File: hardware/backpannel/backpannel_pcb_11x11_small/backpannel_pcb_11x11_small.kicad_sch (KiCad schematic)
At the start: 30 parts, among them J1 Conn_01x02_Female, J2 Conn_02x03, U1 AMS1117-3.3, U2 ESP-12E

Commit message: placement 11x11
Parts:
- S1, S10, S11, S2, S3, S4, S5, S6, S7, S8, S9: footprint woordklok_footprint:WS2812_ledstrip_30leds_meter -> woordklok_footprint:WS2812_ledstrip_60leds_meter
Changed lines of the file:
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@@
     (property "Reference" "S11" (id 0) (at 224.79 120.65 0))
     (property "Value" "WS2812_ledstrip" (id 1) (at 225.26 130.81 0))
-    (property "Footprint" "woordklok_footprint:WS2812_ledstrip_30leds_meter" (id 2) (at 227.33 125.73 0)
+    (property "Footprint" "woordklok_footprint:WS2812_ledstrip_60leds_meter" (id 2) (at 227.33 125.73 0)
       (effects (font (size 1.27 1.27)) hide)
     )
@@
     (property "Reference" "S5" (id 0) (at 226.06 118.11 0))
     (property "Value" "WS2812_ledstrip" (id 1) (at 225.59 107.95 0))
-    (property "Footprint" "woordklok_footprint:WS2812_ledstrip_30leds_meter" (id 2) (at 223.52 113.03 0)
+    (property "Footprint" "woordklok_footprint:WS2812_ledstrip_60leds_meter" (id 2) (at 223.52 113.03 0)
       (effects (font (size 1.27 1.27)) hide)
     )
@@
     (property "Reference" "S9" (id 0) (at 224.79 80.01 0))
     (property "Value" "WS2812_ledstrip" (id 1) (at 225.26 90.17 0))
-    (property "Footprint" "woordklok_footprint:WS2812_ledstrip_30leds_meter" (id 2) (at 227.33 85.09 0)
+    (property "Footprint" "woordklok_footprint:WS2812_ledstrip_60leds_meter" (id 2) (at 227.33 85.09 0)
       (effects (font (size 1.27 1.27)) hide)
     )
@@
     (property "Reference" "S8" (id 0) (at 224.79 59.69 0))
     (property "Value" "WS2812_ledstrip" (id 1) (at 225.26 69.85 0))
-    (property "Footprint" "woordklok_footprint:WS2812_ledstrip_30leds_meter" (id 2) (at 227.33 64.77 0)
+    (property "Footprint" "woordklok_footprint:WS2812_ledstrip_60leds_meter" (id 2) (at 227.33 64.77 0)
       (effects (font (size 1.27 1.27)) hide)
     )
@@
     (property "Reference" "S6" (id 0) (at 226.06 138.43 0))
     (property "Value" "WS2812_ledstrip" (id 1) (at 225.59 128.27 0))
-    (property "Footprint" "woordklok_footprint:WS2812_ledstrip_30leds_meter" (id 2) (at 223.52 133.35 0)
+    (property "Footprint" "woordklok_footprint:WS2812_ledstrip_60leds_meter" (id 2) (at 223.52 133.35 0)
       (effects (font (size 1.27 1.27)) hide)
     )
@@
     (property "Reference" "S7" (id 0) (at 226.06 39.37 0))
     (property "Value" "WS2812_ledstrip" (id 1) (at 224.79 49.53 0))
-    (property "Footprint" "woordklok_footprint:WS2812_ledstrip_30leds_meter" (id 2) (at 227.33 44.45 0)
+    (property "Footprint" "woordklok_footprint:WS2812_ledstrip_60leds_meter" (id 2) (at 227.33 44.45 0)
       (effects (font (size 1.27 1.27)) hide)
     )
@@
     (property "Reference" "S1" (id 0) (at 224.79 36.83 0))
     (property "Value" "WS2812_ledstrip" (id 1) (at 226.06 26.67 0))
-    (property "Footprint" "woordklok_footprint:WS2812_ledstrip_30leds_meter" (id 2) (at 223.52 31.75 0)
+    (property "Footprint" "woordklok_footprint:WS2812_ledstrip_60leds_meter" (id 2) (at 223.52 31.75 0)
       (effects (font (size 1.27 1.27)) hide)
     )
@@
     (property "Reference" "S10" (id 0) (at 224.79 100.33 0))
     (property "Value" "WS2812_ledstrip" (id 1) (at 225.26 110.49 0))
-    (property "Footprint" "woordklok_footprint:WS2812_ledstrip_30leds_meter" (id 2) (at 227.33 105.41 0)
+    (property "Footprint" "woordklok_footprint:WS2812_ledstrip_60leds_meter" (id 2) (at 227.33 105.41 0)
       (effects (font (size 1.27 1.27)) hide)
     )
@@
     (property "Reference" "S2" (id 0) (at 226.06 57.15 0))
     (property "Value" "WS2812_ledstrip" (id 1) (at 225.59 46.99 0))
-    (property "Footprint" "woordklok_footprint:WS2812_ledstrip_30leds_meter" (id 2) (at 223.52 52.07 0)
+    (property "Footprint" "woordklok_footprint:WS2812_ledstrip_60leds_meter" (id 2) (at 223.52 52.07 0)
       (effects (font (size 1.27 1.27)) hide)
     )
@@
     (property "Reference" "S4" (id 0) (at 226.06 97.79 0))
     (property "Value" "WS2812_ledstrip" (id 1) (at 225.59 87.63 0))
-    (property "Footprint" "woordklok_footprint:WS2812_ledstrip_30leds_meter" (id 2) (at 223.52 92.71 0)
+    (property "Footprint" "woordklok_footprint:WS2812_ledstrip_60leds_meter" (id 2) (at 223.52 92.71 0)
       (effects (font (size 1.27 1.27)) hide)
     )
@@
     (property "Reference" "S3" (id 0) (at 226.06 77.47 0))
     (property "Value" "WS2812_ledstrip" (id 1) (at 225.59 67.31 0))
-    (property "Footprint" "woordklok_footprint:WS2812_ledstrip_30leds_meter" (id 2) (at 223.52 72.39 0)
+    (property "Footprint" "woordklok_footprint:WS2812_ledstrip_60leds_meter" (id 2) (at 223.52 72.39 0)
       (effects (font (size 1.27 1.27)) hide)
     )
@@
     )
     (path "/d23aa89d-c621-4b1b-a845-8c26429d6622"
-      (reference "S1") (unit 1) (value "WS2812_ledstrip") (footprint "woordklok_footprint:WS2812_ledstrip_30leds_meter")
+      (reference "S1") (unit 1) (value "WS2812_ledstrip") (footprint "woordklok_footprint:WS2812_ledstrip_60leds_meter")
     )
     (path "/e61e3b10-16bb-45fa-9a42-277efd2ec104"
-      (reference "S2") (unit 1) (value "WS2812_ledstrip") (footprint "woordklok_footprint:WS2812_ledstrip_30leds_meter")
+      (reference "S2") (unit 1) (value "WS2812_ledstrip") (footprint "woordklok_footprint:WS2812_ledstrip_60leds_meter")
     )
     (path "/eef9a49b-90d1-4463-b2c5-af035d3ae9d7"
-      (reference "S3") (unit 1) (value "WS2812_ledstrip") (footprint "woordklok_footprint:WS2812_ledstrip_30leds_meter")
+      (reference "S3") (unit 1) (value "WS2812_ledstrip") (footprint "woordklok_footprint:WS2812_ledstrip_60leds_meter")
     )
     (path "/eec347af-8fb3-4b2d-8e93-6e7176516f57"
-      (reference "S4") (unit 1) (value "WS2812_ledstrip") (footprint "woordklok_footprint:WS2812_ledstrip_30leds_meter")
+      (reference "S4") (unit 1) (value "WS2812_ledstrip") (footprint "woordklok_footprint:WS2812_ledstrip_60leds_meter")
     )
     (path "/40962e92-90b6-487d-b0dc-0a6c42b5ebc2"
-      (reference "S5") (unit 1) (value "WS2812_ledstrip") (footprint "woordklok_footprint:WS2812_ledstrip_30leds_meter")
+      (reference "S5") (unit 1) (value "WS2812_ledstrip") (footprint "woordklok_footprint:WS2812_ledstrip_60leds_meter")
     )
     (path "/5891aa7f-2e48-4492-8db1-d54810991036"
-      (reference "S6") (unit 1) (value "WS2812_ledstrip") (footprint "woordklok_footprint:WS2812_ledstrip_30leds_meter")
+      (reference "S6") (unit 1) (value "WS2812_ledstrip") (footprint "woordklok_footprint:WS2812_ledstrip_60leds_meter")
     )
     (path "/96bdf5ea-ca81-4096-814f-ff6d6aaf3220"
-      (reference "S7") (unit 1) (value "WS2812_ledstrip") (footprint "woordklok_footprint:WS2812_ledstrip_30leds_meter")
+      (reference "S7") (unit 1) (value "WS2812_ledstrip") (footprint "woordklok_footprint:WS2812_ledstrip_60leds_meter")
     )
     (path "/462f8e7e-09c6-4676-ba4f-fd07b2868aa8"
-      (reference "S8") (unit 1) (value "WS2812_ledstrip") (footprint "woordklok_footprint:WS2812_ledstrip_30leds_meter")
+      (reference "S8") (unit 1) (value "WS2812_ledstrip") (footprint "woordklok_footprint:WS2812_ledstrip_60leds_meter")
     )
     (path "/42795956-f125-4166-860d-4316fe3791b8"
-      (reference "S9") (unit 1) (value "WS2812_ledstrip") (footprint "woordklok_footprint:WS2812_ledstrip_30leds_meter")
+      (reference "S9") (unit 1) (value "WS2812_ledstrip") (footprint "woordklok_footprint:WS2812_ledstrip_60leds_meter")
     )
     (path "/d32a1d0f-6a8f-45b4-822f-8b613131fd8a"
-      (reference "S10") (unit 1) (value "WS2812_ledstrip") (footprint "woordklok_footprint:WS2812_ledstrip_30leds_meter")
+      (reference "S10") (unit 1) (value "WS2812_ledstrip") (footprint "woordklok_footprint:WS2812_ledstrip_60leds_meter")
     )
     (path "/21c9358c-c2dd-4df5-9cfe-ea9bd0b49374"
-      (reference "S11") (unit 1) (value "WS2812_ledstrip") (footprint "woordklok_footprint:WS2812_ledstrip_30leds_meter")
+      (reference "S11") (unit 1) (value "WS2812_ledstrip") (footprint "woordklok_footprint:WS2812_ledstrip_60leds_meter")
     )
     (path "/fedb7d4b-8ca2-493c-b9a1-22e781d6d436"

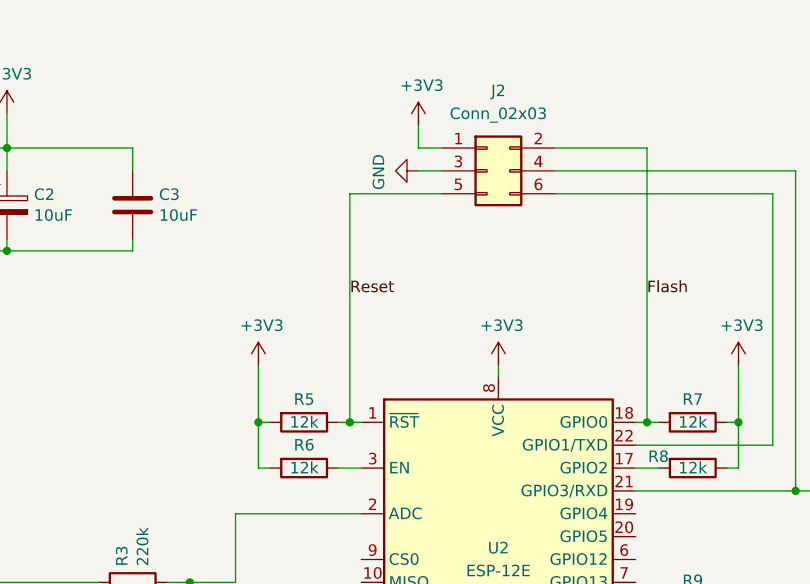
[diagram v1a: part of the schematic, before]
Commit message: finished hardware for small and big clock
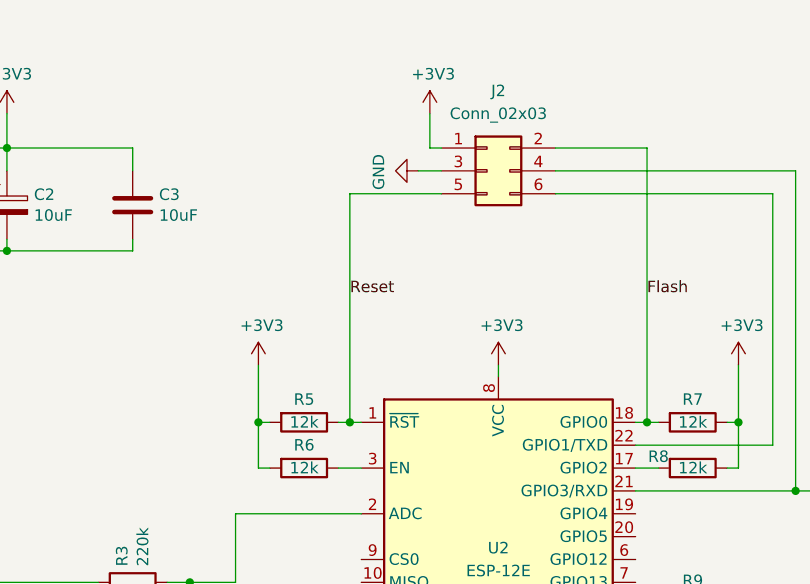
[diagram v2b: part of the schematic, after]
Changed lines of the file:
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@@
+    (stroke (width 0) (type default) (color 0 0 0 0))
+  )
+  (wire (pts (xy 135.89 31.75) (xy 137.16 31.75))
     (stroke (width 0) (type default) (color 0 0 0 0))
   )
@@
     (stroke (width 0) (type default) (color 0 0 0 0))
   )
-  (wire (pts (xy 134.62 31.75) (xy 134.62 29.21))
-    (stroke (width 0) (type default) (color 0 0 0 0))
-  )
   (wire (pts (xy 77.47 43.18) (xy 77.47 46.99))
     (stroke (width 0) (type default) (color 0 0 0 0))
@@
     (stroke (width 0) (type default) (color 0 0 0 0))
   )
+  (wire (pts (xy 173.99 64.77) (xy 173.99 36.83))
+    (stroke (width 0) (type default) (color 0 0 0 0))
+  )
+  (wire (pts (xy 245.11 53.34) (xy 245.11 63.5))
+    (stroke (width 0) (type default) (color 0 0 0 0))
+  )
+  (wire (pts (xy 245.11 93.98) (xy 245.11 104.14))
+    (stroke (width 0) (type default) (color 0 0 0 0))
+  )
+  (wire (pts (xy 55.88 38.1) (xy 55.88 43.18))
+    (stroke (width 0) (type default) (color 0 0 0 0))
+  )
+  (wire (pts (xy 214.63 124.46) (xy 207.01 124.46))
+    (stroke (width 0) (type default) (color 0 0 0 0))
+  )
+  (wire (pts (xy 77.47 80.01) (xy 99.06 80.01))
+    (stroke (width 0) (type default) (color 0 0 0 0))
+  )
+  (wire (pts (xy 214.63 43.18) (xy 207.01 43.18))
+    (stroke (width 0) (type default) (color 0 0 0 0))
+  )
+  (wire (pts (xy 236.22 104.14) (xy 245.11 104.14))
+    (stroke (width 0) (type default) (color 0 0 0 0))
+  )
+  (wire (pts (xy 170.18 67.31) (xy 168.91 67.31))
+    (stroke (width 0) (type default) (color 0 0 0 0))
+  )
+  (wire (pts (xy 109.22 92.71) (xy 109.22 90.17))
+    (stroke (width 0) (type default) (color 0 0 0 0))
+  )
+  (wire (pts (xy 127 36.83) (xy 127 62.23))
+    (stroke (width 0) (type default) (color 0 0 0 0))
+  )
+  (wire (pts (xy 214.63 53.34) (xy 207.01 53.34))
+    (stroke (width 0) (type default) (color 0 0 0 0))
+  )
+  (wire (pts (xy 207.01 104.14) (xy 207.01 114.3))
+    (stroke (width 0) (type default) (color 0 0 0 0))
+  )
+  (wire (pts (xy 143.51 96.52) (xy 143.51 101.6))
+    (stroke (width 0) (type default) (color 0 0 0 0))
+  )
+  (wire (pts (xy 160.02 62.23) (xy 161.29 62.23))
+    (stroke (width 0) (type default) (color 0 0 0 0))
+  )
+  (wire (pts (xy 125.73 62.23) (xy 127 62.23))
+    (stroke (width 0) (type default) (color 0 0 0 0))
+  )
+  (wire (pts (xy 245.11 63.5) (xy 236.22 63.5))
+    (stroke (width 0) (type default) (color 0 0 0 0))
+  )
+  (wire (pts (xy 63.5 31.75) (xy 63.5 27.94))
+    (stroke (width 0) (type default) (color 0 0 0 0))
+  )
+  (wire (pts (xy 207.01 124.46) (xy 207.01 134.62))
+    (stroke (width 0) (type default) (color 0 0 0 0))
+  )
+  (wire (pts (xy 214.63 104.14) (xy 207.01 104.14))
+    (stroke (width 0) (type default) (color 0 0 0 0))
+  )
   (wire (pts (xy 127 36.83) (xy 137.16 36.83))
     (stroke (width 0) (type default) (color 0 0 0 0))
   )
-  (wire (pts (xy 173.99 64.77) (xy 173.99 36.83))
-    (stroke (width 0) (type default) (color 0 0 0 0))
-  )
-  (wire (pts (xy 245.11 53.34) (xy 245.11 63.5))
-    (stroke (width 0) (type default) (color 0 0 0 0))
-  )
-  (wire (pts (xy 245.11 93.98) (xy 245.11 104.14))
-    (stroke (width 0) (type default) (color 0 0 0 0))
-  )
-  (wire (pts (xy 55.88 38.1) (xy 55.88 43.18))
-    (stroke (width 0) (type default) (color 0 0 0 0))
-  )
-  (wire (pts (xy 214.63 124.46) (xy 207.01 124.46))
-    (stroke (width 0) (type default) (color 0 0 0 0))
-  )
-  (wire (pts (xy 77.47 80.01) (xy 99.06 80.01))
-    (stroke (width 0) (type default) (color 0 0 0 0))
-  )
-  (wire (pts (xy 214.63 43.18) (xy 207.01 43.18))
-    (stroke (width 0) (type default) (color 0 0 0 0))
-  )
-  (wire (pts (xy 236.22 104.14) (xy 245.11 104.14))
-    (stroke (width 0) (type default) (color 0 0 0 0))
-  )
-  (wire (pts (xy 170.18 67.31) (xy 168.91 67.31))
-    (stroke (width 0) (type default) (color 0 0 0 0))
-  )
-  (wire (pts (xy 109.22 92.71) (xy 109.22 90.17))
-    (stroke (width 0) (type default) (color 0 0 0 0))
-  )
-  (wire (pts (xy 214.63 53.34) (xy 207.01 53.34))
-    (stroke (width 0) (type default) (color 0 0 0 0))
-  )
-  (wire (pts (xy 207.01 104.14) (xy 207.01 114.3))
-    (stroke (width 0) (type default) (color 0 0 0 0))
-  )
-  (wire (pts (xy 143.51 96.52) (xy 143.51 101.6))
-    (stroke (width 0) (type default) (color 0 0 0 0))
-  )
-  (wire (pts (xy 160.02 62.23) (xy 161.29 62.23))
-    (stroke (width 0) (type default) (color 0 0 0 0))
-  )
-  (wire (pts (xy 125.73 62.23) (xy 127 62.23))
-    (stroke (width 0) (type default) (color 0 0 0 0))
-  )
-  (wire (pts (xy 245.11 63.5) (xy 236.22 63.5))
-    (stroke (width 0) (type default) (color 0 0 0 0))
-  )
-  (wire (pts (xy 63.5 31.75) (xy 63.5 27.94))
-    (stroke (width 0) (type default) (color 0 0 0 0))
-  )
-  (wire (pts (xy 207.01 124.46) (xy 207.01 134.62))
-    (stroke (width 0) (type default) (color 0 0 0 0))
-  )
-  (wire (pts (xy 214.63 104.14) (xy 207.01 104.14))
-    (stroke (width 0) (type default) (color 0 0 0 0))
-  )
   (wire (pts (xy 242.57 33.02) (xy 242.57 43.18))
     (stroke (width 0) (type default) (color 0 0 0 0))
@@
     (stroke (width 0) (type default) (color 0 0 0 0))
   )
-  (wire (pts (xy 127 62.23) (xy 127 36.83))
-    (stroke (width 0) (type default) (color 0 0 0 0))
-  )
   (wire (pts (xy 55.88 43.18) (xy 63.5 43.18))
     (stroke (width 0) (type default) (color 0 0 0 0))
@@
     (stroke (width 0) (type default) (color 0 0 0 0))
   )
+  (wire (pts (xy 135.89 27.94) (xy 135.89 31.75))
+    (stroke (width 0) (type default) (color 0 0 0 0))
+  )
   (wire (pts (xy 44.45 35.56) (xy 50.8 35.56))
     (stroke (width 0) (type default) (color 0 0 0 0))
@@
   )
   (wire (pts (xy 63.5 31.75) (xy 68.58 31.75))
-    (stroke (width 0) (type default) (color 0 0 0 0))
-  )
-  (wire (pts (xy 137.16 31.75) (xy 134.62 31.75))
     (stroke (width 0) (type default) (color 0 0 0 0))
   )
@@
     (pin "1")
   )
-  (symbol (lib_id "power:+3V3") (at 134.62 29.21 0) (unit 1)
-    (in_bom yes) (on_board yes)
-    (property "Reference" "#PWR0124" (id 0) (at 134.62 33.02 0)
-      (effects (font (size 1.27 1.27)) hide)
-    )
-    (property "Value" "+3V3" (id 1) (at 135.001 24.8158 0))
-    (property "Footprint" "" (id 2) (at 134.62 29.21 0)
-      (effects (font (size 1.27 1.27)) hide)
-    )
-    (property "Datasheet" "" (id 3) (at 134.62 29.21 0)
-      (effects (font (size 1.27 1.27)) hide)
-    )
+  (symbol (lib_id "power:+3V3") (at 135.89 27.94 0) (unit 1)
+    (in_bom yes) (on_board yes)
+    (property "Reference" "#PWR0124" (id 0) (at 135.89 31.75 0)
+      (effects (font (size 1.27 1.27)) hide)
+    )
+    (property "Value" "+3V3" (id 1) (at 136.271 23.5458 0))
+    (property "Footprint" "" (id 2) (at 135.89 27.94 0)
+      (effects (font (size 1.27 1.27)) hide)
+    )
+    (property "Datasheet" "" (id 3) (at 135.89 27.94 0)
+      (effects (font (size 1.27 1.27)) hide)
+    )
